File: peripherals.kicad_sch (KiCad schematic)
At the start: 80 parts, among them J2 Screw_Terminal_01x06, J3 Screw_Terminal_01x03, J5 Screw_Terminal_01x03, J8 Screw_Terminal_01x04, K1 FINDER-32.21-x000, K2 FINDER-32.21-x000, Q10 BC847BDW1, Q2 BSS138DW, Q3 BSS138DW, Q4 IRLML9301, Q6 BSS138DW, Q9 IRLML9301, T11 3V3, T4 IN2, T5 IN1, T7 IN3, T8 IN4, U16 MCP23S08-xML, U3 74LVC2G14, U4 74LVC2G14

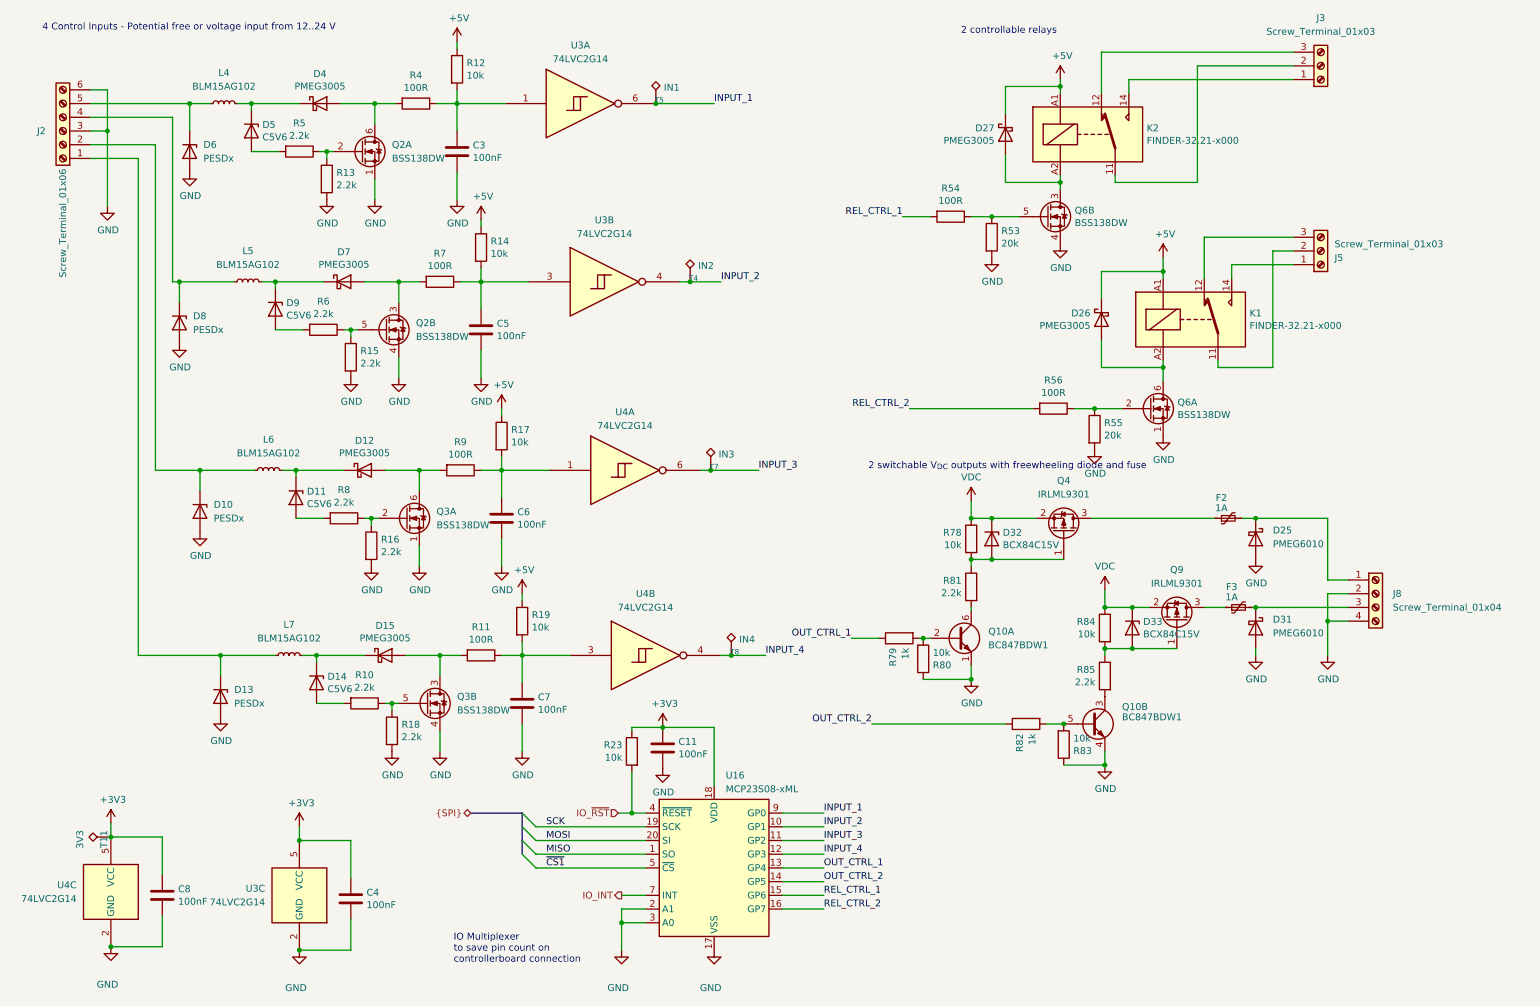
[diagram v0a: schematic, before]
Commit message: Simplified design (Old version switched to hodor-max)
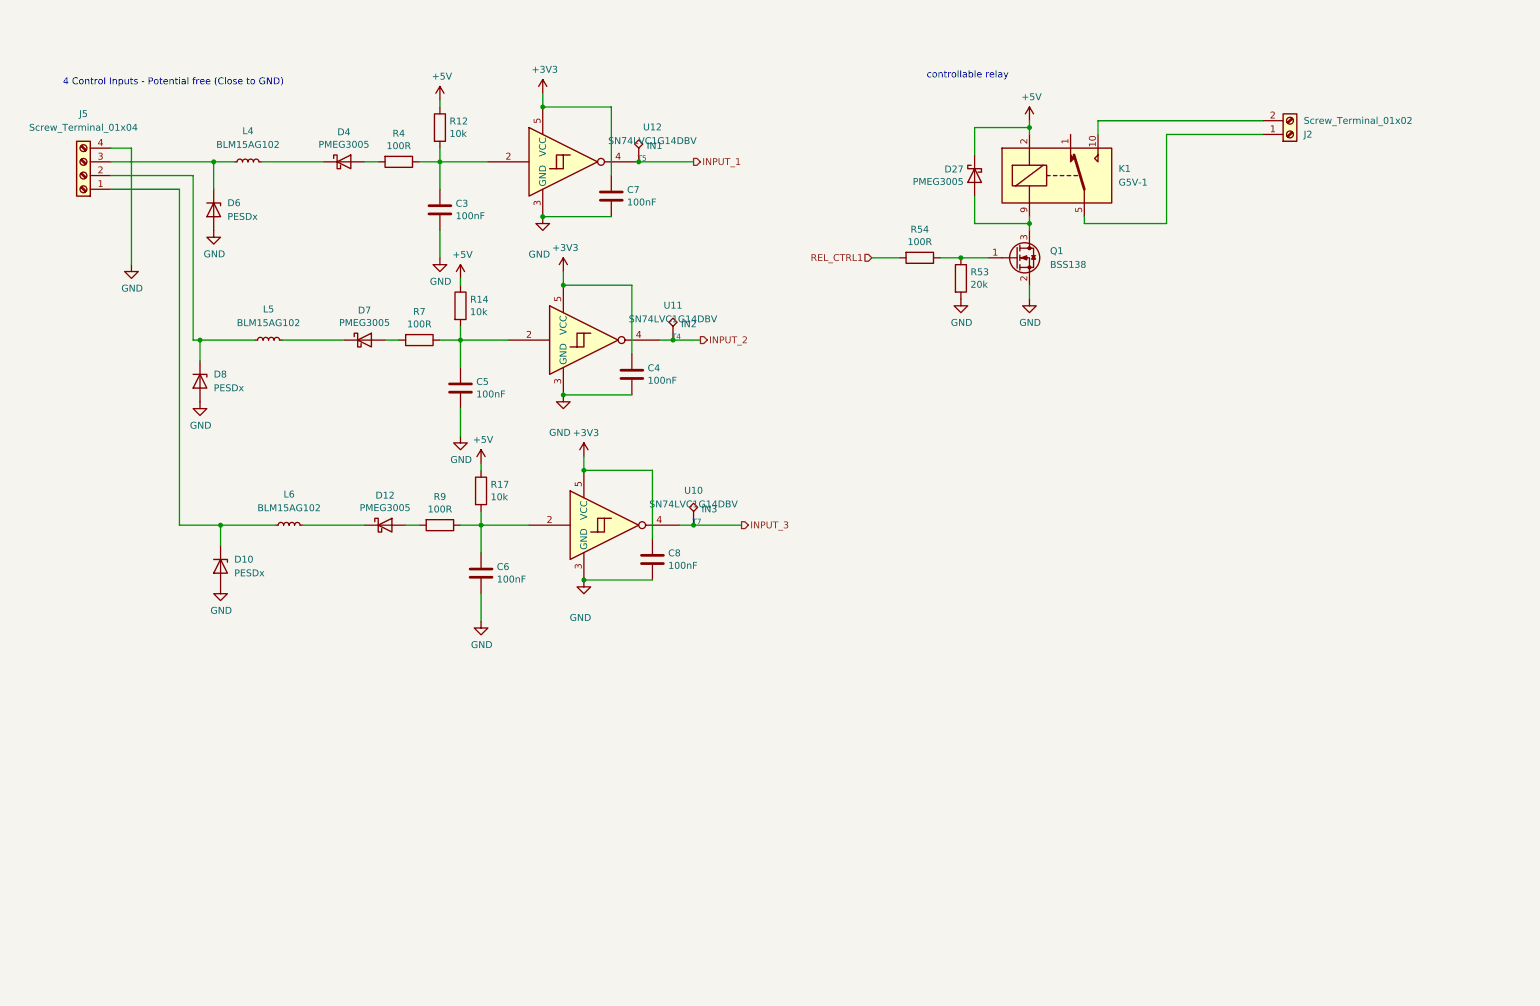
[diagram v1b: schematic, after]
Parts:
- removed C11: 100nF, Capacitor_SMD:C_0402_1005Metric, symbol Device:C
- removed D11, D14, D5, D9: C5V6, Diode_SMD:D_SOD-523, symbol Device:D_Zener
- removed D13: PESDx, Diode_SMD:D_SOD-523, symbol Diode:PTVS26VZ1USK
- removed D15, D26: PMEG3005, Diode_SMD:D_SOD-523, symbol Device:D_Schottky
- removed D25, D31: PMEG6010, Diode_SMD:D_SOD-123F, symbol Device:D_Schottky
- removed D32, D33: BCX84C15V, Diode_SMD:D_SOD-523, symbol Device:D_Zener
- removed F2, F3: 1A, Fuse:Fuse_1210_3225Metric, symbol Device:Polyfuse_Small
- removed J2: Screw_Terminal_01x06, TerminalBlock_Phoenix:TerminalBlock_Phoenix_MKDS-1,5-6_1x06_P5.00mm_Horizontal, symbol Connector:Screw_Terminal_01x06
- removed J3, J5: Screw_Terminal_01x03, TerminalBlock_Phoenix:TerminalBlock_Phoenix_MKDS-1,5-3_1x03_P5.00mm_Horizontal, symbol Connector:Screw_Terminal_01x03
- removed J8: Screw_Terminal_01x04, TerminalBlock_Phoenix:TerminalBlock_Phoenix_MKDS-1,5-4_1x04_P5.00mm_Horizontal, symbol Connector:Screw_Terminal_01x04
- removed K1, K2: FINDER-32.21-x000, Relay_THT:Relay_SPDT_Finder_32.21-x000, symbol Relay:FINDER-32.21-x000
- removed L7: BLM15AG102, Inductor_SMD:L_0402_1005Metric, symbol Device:L_Small
- removed Q10: BC847BDW1, Package_TO_SOT_SMD:SOT-363_SC-70-6, symbol Transistor_BJT:BC847BDW1
- removed Q2, Q3, Q6: BSS138DW, Package_TO_SOT_SMD:SOT-363_SC-70-6, symbol Transistor_FET:FDG1024NZ
- removed Q4, Q9: IRLML9301, Package_TO_SOT_SMD:SOT-23, symbol Transistor_FET:IRLML9301
- removed R10, R13, R15, R16, R18, R5, R6, R8, R81, R85: 2.2k, Resistor_SMD:R_0402_1005Metric, symbol Device:R
- removed R11, R56: 100R, Resistor_SMD:R_0402_1005Metric, symbol Device:R
- removed R19, R23, R78, R80, R83, R84: 10k, Resistor_SMD:R_0402_1005Metric, symbol Device:R
- removed R55: 20k, Resistor_SMD:R_0402_1005Metric, symbol Device:R
- removed R79, R82: 1k, Resistor_SMD:R_0402_1005Metric, symbol Device:R
- removed T11: 3V3, TestPoint:TestPoint_Pad_D1.0mm, symbol Connector:TestPoint_Alt
- removed T8: IN4, TestPoint:TestPoint_Pad_D1.0mm, symbol Connector:TestPoint_Alt
- removed U16: MCP23S08-xML, Package_DFN_QFN:QFN-20-1EP_4x4mm_P0.5mm_EP2.7x2.7mm, symbol hodor_custom_parts:MCP23S08-xML
- removed U3, U4: 74LVC2G14, Package_TO_SOT_SMD:SOT-23-6, symbol 74xGxx:74LVC2G14
- added J2: Screw_Terminal_01x02, TerminalBlock_Phoenix:TerminalBlock_Phoenix_MKDS-1,5-2_1x02_P5.00mm_Horizontal, symbol Connector:Screw_Terminal_01x02
- added J5: Screw_Terminal_01x04, TerminalBlock_Phoenix:TerminalBlock_Phoenix_MKDS-1,5-4_1x04_P5.00mm_Horizontal, symbol Connector:Screw_Terminal_01x04
- added K1: G5V-1, Relay_THT:Relay_SPDT_Omron_G5V-1, symbol Relay:G5V-1
- added Q1: BSS138, Package_TO_SOT_SMD:SOT-23, symbol Transistor_FET:BSS138
- added U10, U11, U12: SN74LVC1G14DBV, Package_TO_SOT_SMD:SOT-23-5, symbol 74xGxx:SN74LVC1G14DBV
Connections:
- net +3V3: now also C7.1, U10.5 (VCC), U11.5 (VCC), U12.5 (VCC)
- net +5V: now also K1.2
- net GND: now also J5.4 (Pin_4), Q1.2 (S), U10.3 (GND), U11.3 (GND), U12.3 (GND)
- net INPUT_1: now also U12.4
- net INPUT_2: now also U11.4
- net INPUT_3: now also U10.4
- net at D27.2 (A): now also K1.9, Q1.3 (D)
- net at R53.1, R54.1: now also Q1.1 (G)
- net at C3.1, R12.2, R4.1: now also U12.2
- net at C5.1, R14.2, R7.1: now also U11.2
- net at C6.1, R17.2, R9.1: now also U10.2
- net at D6.1 (K), L4.1: now also J5.3 (Pin_3)
- net at D8.1 (K), L5.1: now also J5.2 (Pin_2)
- net at D10.1 (K), L6.1: now also J5.1 (Pin_1)
- net REL_CTRL_1 renamed REL_CTRL1
- new net: J2.2 (Pin_2), K1.10
- new net: J2.1 (Pin_1), K1.5, K1.6
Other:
- note added: "4 Control Inputs - Potential free (Close to GND)"
- note added: "controllable relay"
- note removed: "2 controllable relays"
- note removed: "2 switchable V_{DC} outputs with freewheeling diode and fuse"
- note removed: "4 Control Inputs - Potential free or voltage input from 12..24 V"
- note removed: "IO Multiplexer to save pin count on controllerboard connection"
- moved on the sheet: C3, C5, C6, C8, D10, D12, D27, D4, D6, D7, D8, L4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

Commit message: Finalized Layout
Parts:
- renumbered C3 to C1, C5 to C2, C6 to C3, C7 to C5, C4 to C6, C8 to C7, D6 to D1, D8 to D2, D10 to D3, D4 to D5, D7 to D6, D12 to D7, D27 to D9, J5 to J2, J2 to J3, L4 to L1, L5 to L2, L6 to L3, R4 to R1, R54 to R10, R12 to R2, R14 to R3, R7 to R4, R9 to R5, R17 to R6, R53 to R9, T5 to T3, T7 to T5, U12 to U1, U11 to U2, U10 to U3
